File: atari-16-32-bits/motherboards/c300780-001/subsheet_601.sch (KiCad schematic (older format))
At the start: 11 parts, among them P600 10K ×8, U632 74LS244_PHY

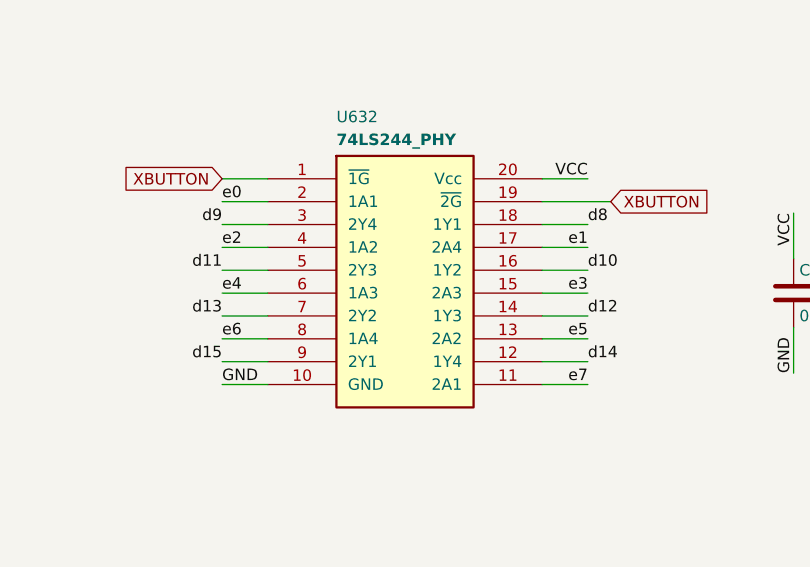
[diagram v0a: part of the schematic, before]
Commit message: Fixed : [ERC] wrong case for labels between bus and pins
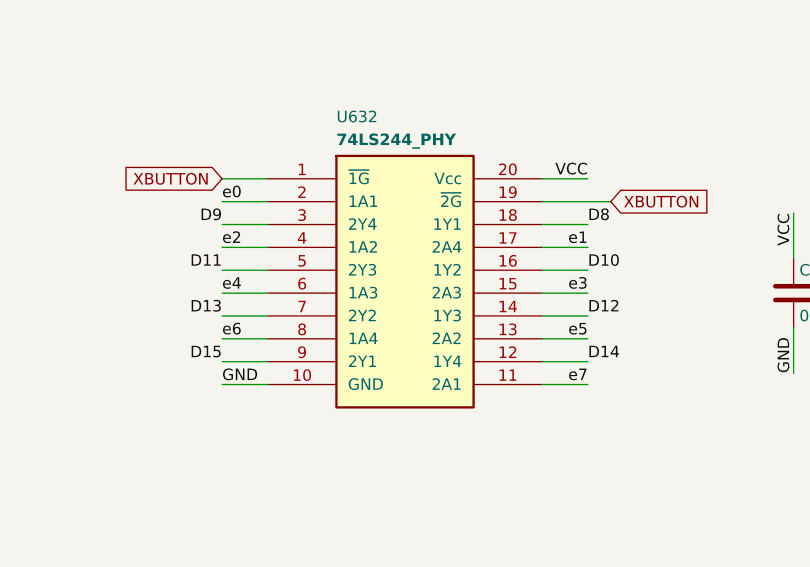
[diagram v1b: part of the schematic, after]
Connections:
- net d10 renamed D10
- net d11 renamed D11
- net d12 renamed D12
- net d13 renamed D13
- net d14 renamed D14
- net d15 renamed D15
- net d8 renamed D8
- net d9 renamed D9
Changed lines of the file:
@@
 	6100 2800 5900 2800
 Text Label 6100 2200 0    50   ~ 0
-d8
+D8
 Text Label 4500 2200 2    50   ~ 0
-d9
+D9
 Text Label 6100 2400 0    50   ~ 0
-d10
+D10
 Text Label 4500 2400 2    50   ~ 0
-d11
+D11
 Text Label 6100 2600 0    50   ~ 0
-d12
+D12
 Text Label 4500 2600 2    50   ~ 0
-d13
+D13
 Text Label 6100 2800 0    50   ~ 0
-d14
+D14
 Text Label 4500 2800 2    50   ~ 0
-d15
+D15
 Wire Wire Line
 	5900 2100 6200 2100
